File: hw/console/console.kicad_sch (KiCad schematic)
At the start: 155 parts, among them J1 Batt, J301 USB-C 16P, J401 microSD push-push, J501 SPK 8R, J601 FFC-40 0.5mm, J901 UART, Q601 N-MOSFET, SW1 Движок, SW101 UP, SW102 DOWN, SW103 LEFT, SW104 RIGHT, SW105 SELECT, SW106 START, SW107 A, SW108 B, SW109 C, SW110 D, SW2 RESET, SW301 FEL, U1 F133-A, U2 SY8089AAAC, U3 SY8089AAAC, U4 SY8089AAAC, U401 W25Q32JVSSIQ, U5 TP4056, U501 PAM8301, Y1 24 МГц, Y2 32.768 кГц

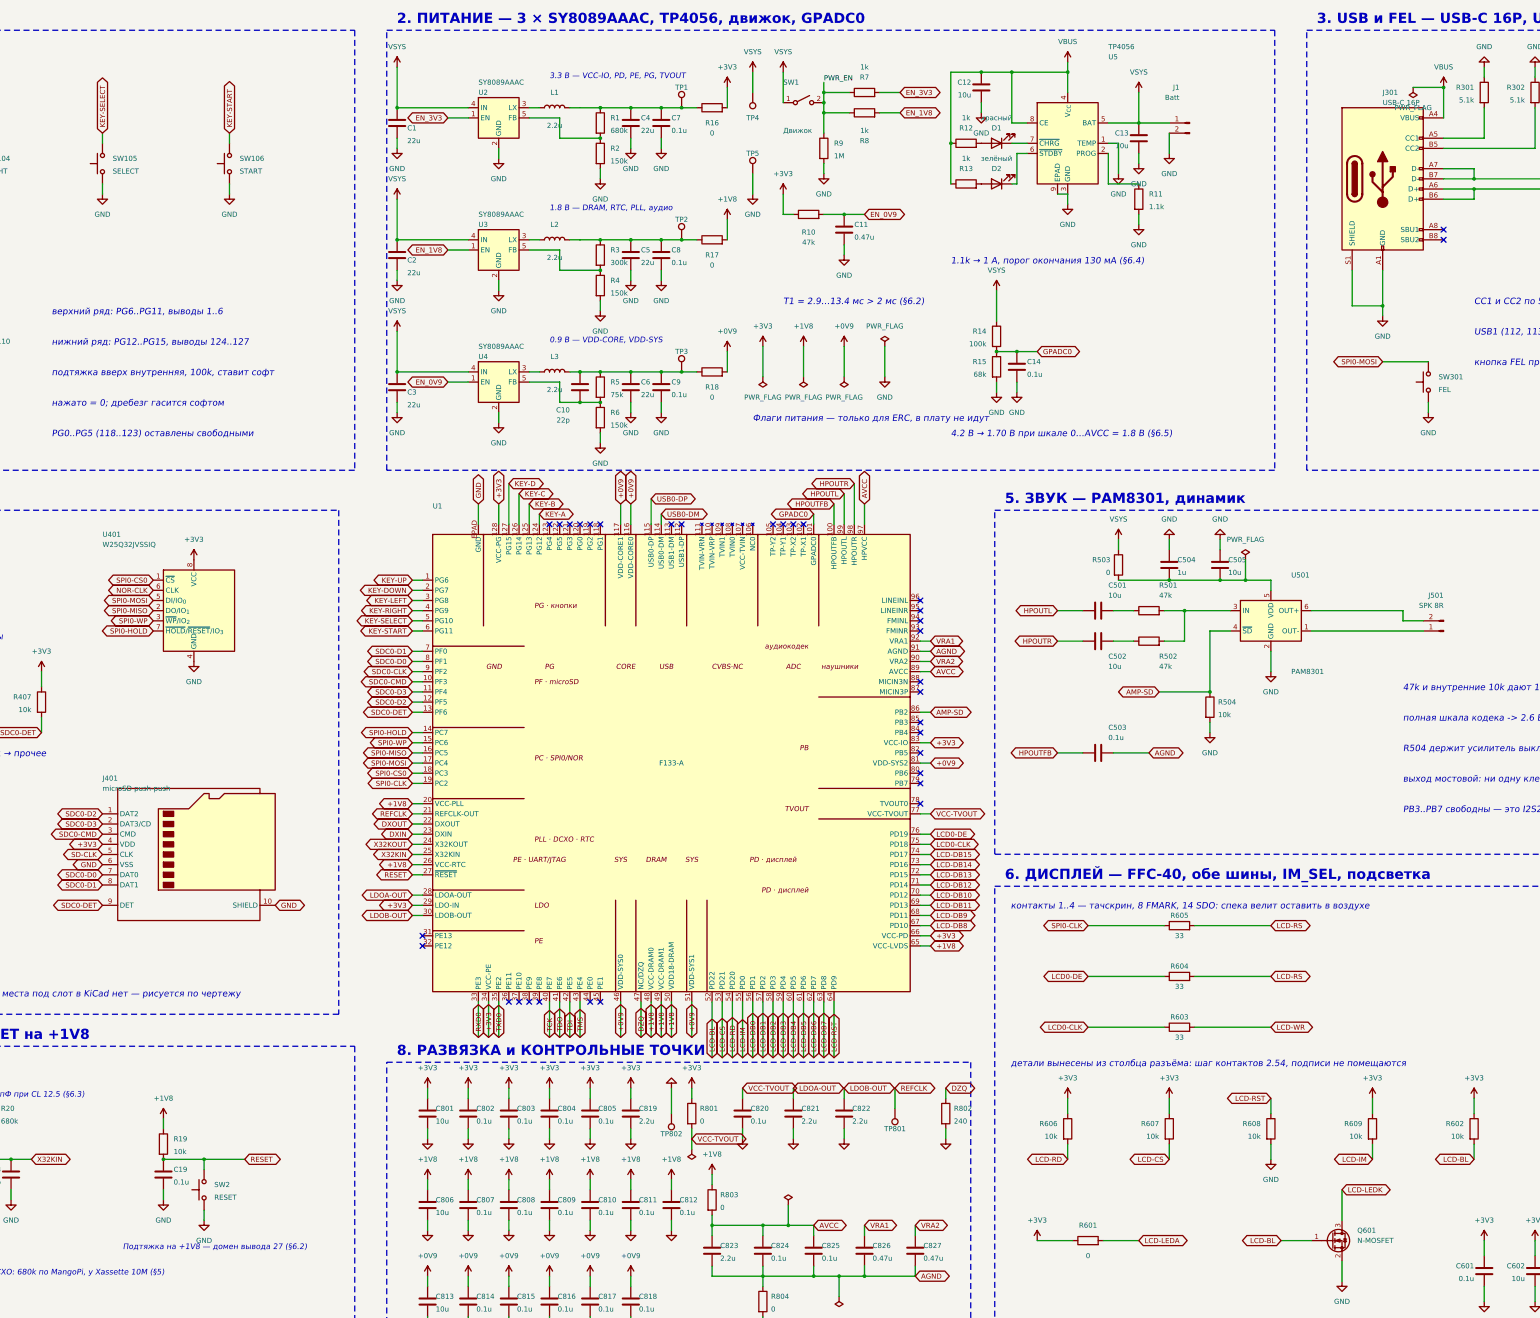
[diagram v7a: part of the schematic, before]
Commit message: hw: закрыты последние шесть деталей без корпуса, FEL и RESET стали площадками
Схема была полной, но у шести деталей не было посадочного места, и это
блокировало плату. Теперь корпус есть у всех 155.

Дроссели L1..L3 — Sunlord SWPA3015S2R2NT. Планка «ISAT >= 2 A, DCR < 50 мОм»
из 02-power.md §6.1 оказалась нашей же перестраховкой: расчёт в §7.2 требует
0.76 А, а живая плата Xassette работает на 176 мОм, втрое хуже рекомендации
даташита. Расхождение записано в §5 вместе с ценой вопроса — 0.1 Вт на трёх
каналах. Высоту 1.5 мм выбрали сознательно: на изнанке лежит банка.

Q601 — AO3400A, требования §7.1 закрыты таблицей по даташиту AOS.
SW1 — Shouhan MSK-12C02, символ сменён на SW_SPDT: деталь трёхвыводная.

J401 — Hirose DM3AT-SF-PEJM5 вместо безымянного C393941. Дороже в 14 раз,
зато закрывает три вопроса разом: символ и корпус в KiCad готовые и совпадают
по партномеру, а полярность детектора описана в каталоге («без карты Open,
карта вставлена Closed») вместо того, чтобы звонить её тестером.

J601 — свой корпус FH12-40S-0.5SH_ContactsReversed. Геометрия побайтово из
штатного Hirose, переставлены только номера площадок. Причина в §7.2.1:
хвост панели заворачивается на 180 градусов ей на изнанку и приходит к
разъёму в обратном порядке, а отзеркалить корпус на той же стороне платы
нечем. Все пять футпринтов KiCad на 40 контактов 0.5 мм — одной «рукости».

FEL и RESET — больше не кнопки, а пары контактных площадок под пинцет.
У Xassette кнопок нет ни одной, серийные консоли кнопки сброса не носят
вовсе, а в FEL входят картой с fel-sdboot.sunxi или замыканием площадки.
Плюс у нас страпы дают SMHC0 первым приоритетом, то есть карта с валидным
boot0 поднимет плату и с убитой флешкой (04-storage.md §6.4). Правка ТЗ
внесена. Побочно: с изнанки ушли две детали высотой 4.3 мм.

ERC ноль, все шестнадцать проверок audit.py ноль.

Co-Authored-By: Claude Opus 5 <noreply@anthropic.com>
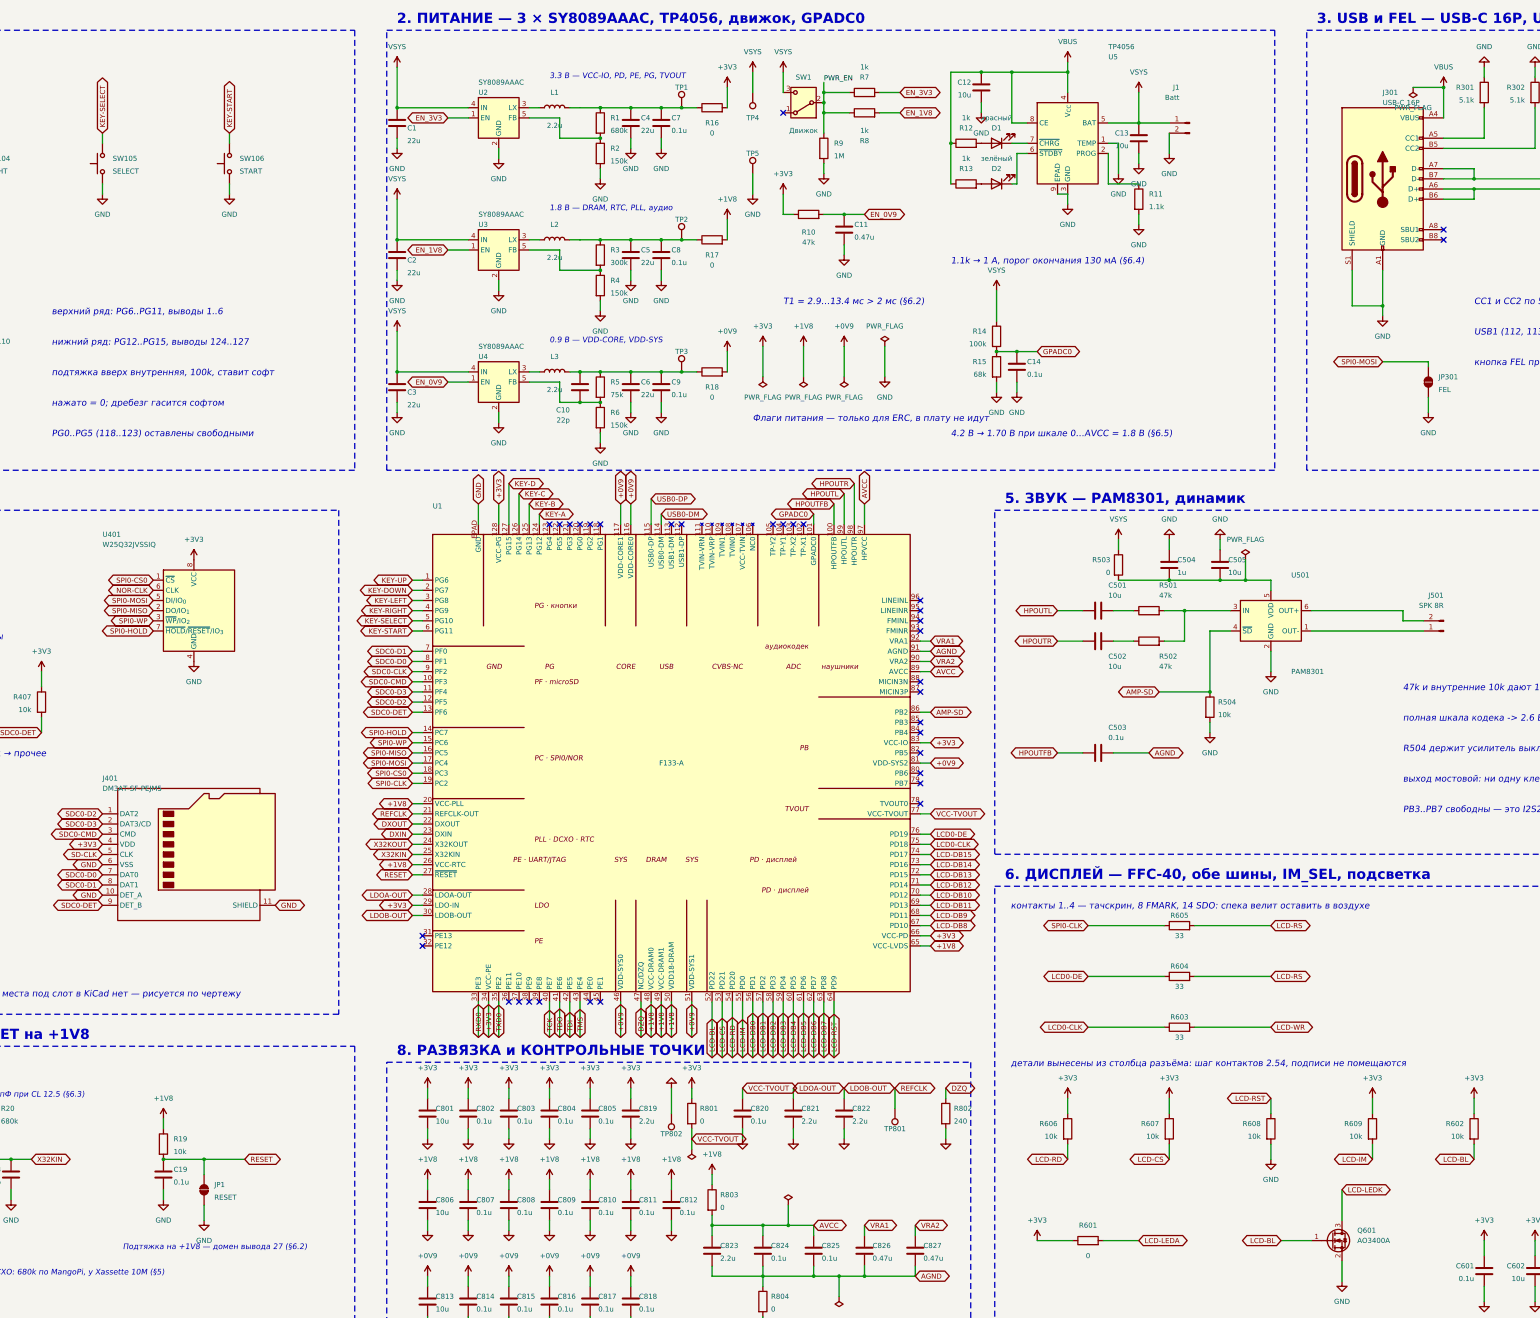
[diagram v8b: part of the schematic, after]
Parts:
- removed SW2: RESET, Button_Switch_SMD:SW_SPST_PTS645Sx43SMTR92, symbol Switch:SW_Push
- removed SW301: FEL, Button_Switch_SMD:SW_SPST_PTS645Sx43SMTR92, symbol Switch:SW_Push
- added JP1: RESET, Jumper:SolderJumper-2_P1.3mm_Open_Pad1.0x1.5mm, symbol Jumper:SolderJumper_2_Open
- added JP301: FEL, Jumper:SolderJumper-2_P1.3mm_Open_Pad1.0x1.5mm, symbol Jumper:SolderJumper_2_Open
- J401: value microSD push-push -> DM3AT-SF-PEJM5; footprint (none) -> Connector_Card:microSD_HC_Hirose_DM3AT-SF-PEJM5; symbol Connector:Micro_SD_Card_Det1 -> Connector:Micro_SD_Card_Det_Hirose_DM3AT; LCSC C393941 -> C114218
- J601: footprint Connector_FFC-FPC:Hirose_FH12-40S-0.5SH_1x40-1MP_P0.50mm_Horizontal -> console:FH12-40S-0.5SH_ContactsReversed; Источник 06-display.md §6.1 -> 06-display.md §6.1, §7.2
- L1, L2, L3: footprint (none) -> Inductor_SMD:L_Sunlord_SWPA3015S
- Q601: value N-MOSFET -> AO3400A; footprint (none) -> Package_TO_SOT_SMD:SOT-23
- SW1: footprint (none) -> Button_Switch_SMD:SW_SPDT_Shouhan_MSK12C02; symbol Switch:SW_SPST -> Switch:SW_SPDT
- U5: footprint Package_SO:SOIC-8-1EP_3.9x4.9mm_P1.27mm_EP2.41x3.3mm_ThermalVias -> Package_SO:SOIC-8-1EP_3.9x4.9mm_P1.27mm_EP2.41x3.3mm
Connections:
- net GND: now also J401.11 (SHIELD), JP1.1 (A), JP301.1 (A)
- net RESET: now also JP1.2 (B)
- net SPI0-MOSI: now also JP301.2 (B)
- net VSYS: now also SW1.3 (C); no longer SW1.1 (A)
- no-connect marks 40 -> 41
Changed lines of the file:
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@@
 			)
 		)
-		(property "Footprint" ""
+		(property "Footprint" "Inductor_SMD:L_Sunlord_SWPA3015S"
 			(at 267.97 39.37 0)
 			(effects
@@
 			)
 		)
-		(property "Footprint" ""
+		(property "Footprint" "Inductor_SMD:L_Sunlord_SWPA3015S"
 			(at 267.97 72.39 0)
 			(effects
@@
 			)
 		)
-		(property "Footprint" ""
+		(property "Footprint" "Inductor_SMD:L_Sunlord_SWPA3015S"
 			(at 267.97 105.41 0)
 			(effects
@@
 	)
 	(symbol
-		(lib_id "Switch:SW_SPST")
-		(at 330.2 38.1 0)
+		(lib_id "Switch:SW_SPDT")
+		(at 330.2 38.1 180)
 		(unit 1)
 		(exclude_from_sim no)
@@
 		(dnp no)
 		(property "Reference" "SW1"
-			(at 325.12 33.02 0)
+			(at 330.2 31.75 0)
 			(effects
 				(font (size 1.27 1.27))
-				(justify left)
 			)
 		)
 		(property "Value" "Движок"
-			(at 325.12 45.09 0)
+			(at 330.2 45.09 0)
 			(effects
 				(font (size 1.27 1.27))
-				(justify left)
 			)
 		)
-		(property "Footprint" ""
+		(property "Footprint" "Button_Switch_SMD:SW_SPDT_Shouhan_MSK12C02"
 			(at 330.2 38.1 0)
 			(effects
@@
 	)
 	(wire
-		(pts (xy 325.12 30.48) (xy 325.12 38.1))
+		(pts (xy 325.12 30.48) (xy 325.12 35.56))
 		(stroke (width 0) (type default))
 	)
+	(no_connect
+		(at 325.12 40.64)
+	)
 	(wire
 		(pts (xy 335.28 33.02) (xy 335.28 35.56))
@@
 			)
 		)
-		(property "Footprint" "Package_SO:SOIC-8-1EP_3.9x4.9mm_P1.27mm_EP2.41x3.3mm_ThermalVias"
+		(property "Footprint" "Package_SO:SOIC-8-1EP_3.9x4.9mm_P1.27mm_EP2.41x3.3mm"
 			(at 396.24 48.26 0)
 			(effects
@@
 		(effects (font (size 1.27 1.27)) (justify left))
 	)
-	(global_label "SPI0-MOSI"
-		(shape bidirectional)
-		(at 474.98 102.87 180)
-		(effects (font (size 1.27 1.27)) (justify right))
-	)
-	(wire
-		(pts (xy 474.98 102.87) (xy 486.41 102.87))
-		(stroke (width 0) (type default))
-	)
 	(symbol
-		(lib_id "Switch:SW_Push")
+		(lib_id "Jumper:SolderJumper_2_Open")
 		(at 486.41 107.95 90)
 		(unit 1)
@@
 		(on_board yes)
 		(dnp no)
-		(property "Reference" "SW301"
+		(property "Reference" "JP301"
 			(at 488.95 106.68 270)
 			(effects
@@
 			)
 		)
-		(property "Footprint" "Button_Switch_SMD:SW_SPST_PTS645Sx43SMTR92"
+		(property "Footprint" "Jumper:SolderJumper-2_P1.3mm_Open_Pad1.0x1.5mm"
 			(at 486.41 107.95 0)
 			(effects
@@
 			(project "console"
 				(path "/2c95ea68-c905-5549-acc9-040ef4143065"
-					(reference "SW301")
+					(reference "JP301")
 					(unit 1)
 				)
@@
 		)
 	)
+	(global_label "SPI0-MOSI"
+		(shape bidirectional)
+		(at 474.98 102.87 180)
+		(effects (font (size 1.27 1.27)) (justify right))
+	)
 	(wire
-		(pts (xy 486.41 113.03) (xy 486.41 115.57))
+		(pts (xy 474.98 102.87) (xy 486.41 102.87))
+		(stroke (width 0) (type default))
+	)
+	(wire
+		(pts (xy 486.41 102.87) (xy 486.41 104.14))
+		(stroke (width 0) (type default))
+	)
+	(wire
+		(pts (xy 486.41 111.76) (xy 486.41 115.57))
 		(stroke (width 0) (type default))
 	)
@@
 	)
 	(symbol
-		(lib_id "Connector:Micro_SD_Card_Det1")
+		(lib_id "Connector:Micro_SD_Card_Det_Hirose_DM3AT")
 		(at 177.8 226.06 0)
 		(unit 1)
@@
 			)
 		)
-		(property "Value" "microSD push-push"
+		(property "Value" "DM3AT-SF-PEJM5"
 			(at 154.94 209.55 0)
 			(effects
@@
 			)
 		)
-		(property "Footprint" ""
+		(property "Footprint" "Connector_Card:microSD_HC_Hirose_DM3AT-SF-PEJM5"
 			(at 177.8 226.06 0)
 			(effects
@@
 			)
 		)
-		(property "LCSC" "C393941"
+		(property "LCSC" "C114218"
 			(at 177.8 226.06 0)
 			(effects
@@
 	(global_label "GND"
 		(shape bidirectional)
+		(at 154.94 236.22 180)
+		(effects (font (size 1.27 1.27)) (justify right))
+	)
+	(global_label "GND"
+		(shape bidirectional)
 		(at 198.12 238.76 0)
 		(effects (font (size 1.27 1.27)) (justify left))
@@
 			)
 		)
-		(property "Footprint" "Connector_FFC-FPC:Hirose_FH12-40S-0.5SH_1x40-1MP_P0.50mm_Horizontal"
+		(property "Footprint" "console:FH12-40S-0.5SH_ContactsReversed"
 			(at 546.1 285.75 0)
 			(effects
@@
 			)
 		)
-		(property "Источник" "06-display.md §6.1"
+		(property "Источник" "06-display.md §6.1, §7.2"
 			(at 546.1 285.75 0)
 			(effects
@@
 			)
 		)
-		(property "Value" "N-MOSFET"
+		(property "Value" "AO3400A"
 			(at 468.63 322.58 0)
 			(effects
@@
 			)
 		)
-		(property "Footprint" ""
+		(property "Footprint" "Package_TO_SOT_SMD:SOT-23"
 			(at 462.28 322.58 0)
 			(effects
@@
 	)
 	(symbol
-		(lib_id "Switch:SW_Push")
+		(lib_id "Jumper:SolderJumper_2_Open")
 		(at 180.34 309.88 90)
 		(unit 1)
@@
 		(on_board yes)
 		(dnp no)
-		(property "Reference" "SW2"
+		(property "Reference" "JP1"
 			(at 182.88 308.61 270)
 			(effects
@@
 			)
 		)
-		(property "Footprint" "Button_Switch_SMD:SW_SPST_PTS645Sx43SMTR92"
+		(property "Footprint" "Jumper:SolderJumper-2_P1.3mm_Open_Pad1.0x1.5mm"
 			(at 180.34 309.88 0)
 			(effects
@@
 			(project "console"
 				(path "/2c95ea68-c905-5549-acc9-040ef4143065"
-					(reference "SW2")
+					(reference "JP1")
 					(unit 1)
 				)
@@
 	)
 	(wire
-		(pts (xy 180.34 302.26) (xy 180.34 304.8))
+		(pts (xy 180.34 302.26) (xy 180.34 306.07))
 		(stroke (width 0) (type default))
 	)
 	(wire
-		(pts (xy 180.34 314.96) (xy 180.34 317.5))
+		(pts (xy 180.34 313.69) (xy 180.34 317.5))
 		(stroke (width 0) (type default))
 	)
